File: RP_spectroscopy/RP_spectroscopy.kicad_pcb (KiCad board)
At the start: 2 copper layers, 90.5 x 110 mm, 82 parts, among them J1 Extension connector 1, J2 Extension connector 2, J3 Conn_Coaxial, J4 Conn_Coaxial, J5 Conn_Coaxial, J6 Conn_Coaxial, J7 Conn_01x04_MountingPin, J8 Conn_01x04_MountingPin, U1 AD8603, U2 ADG417BR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

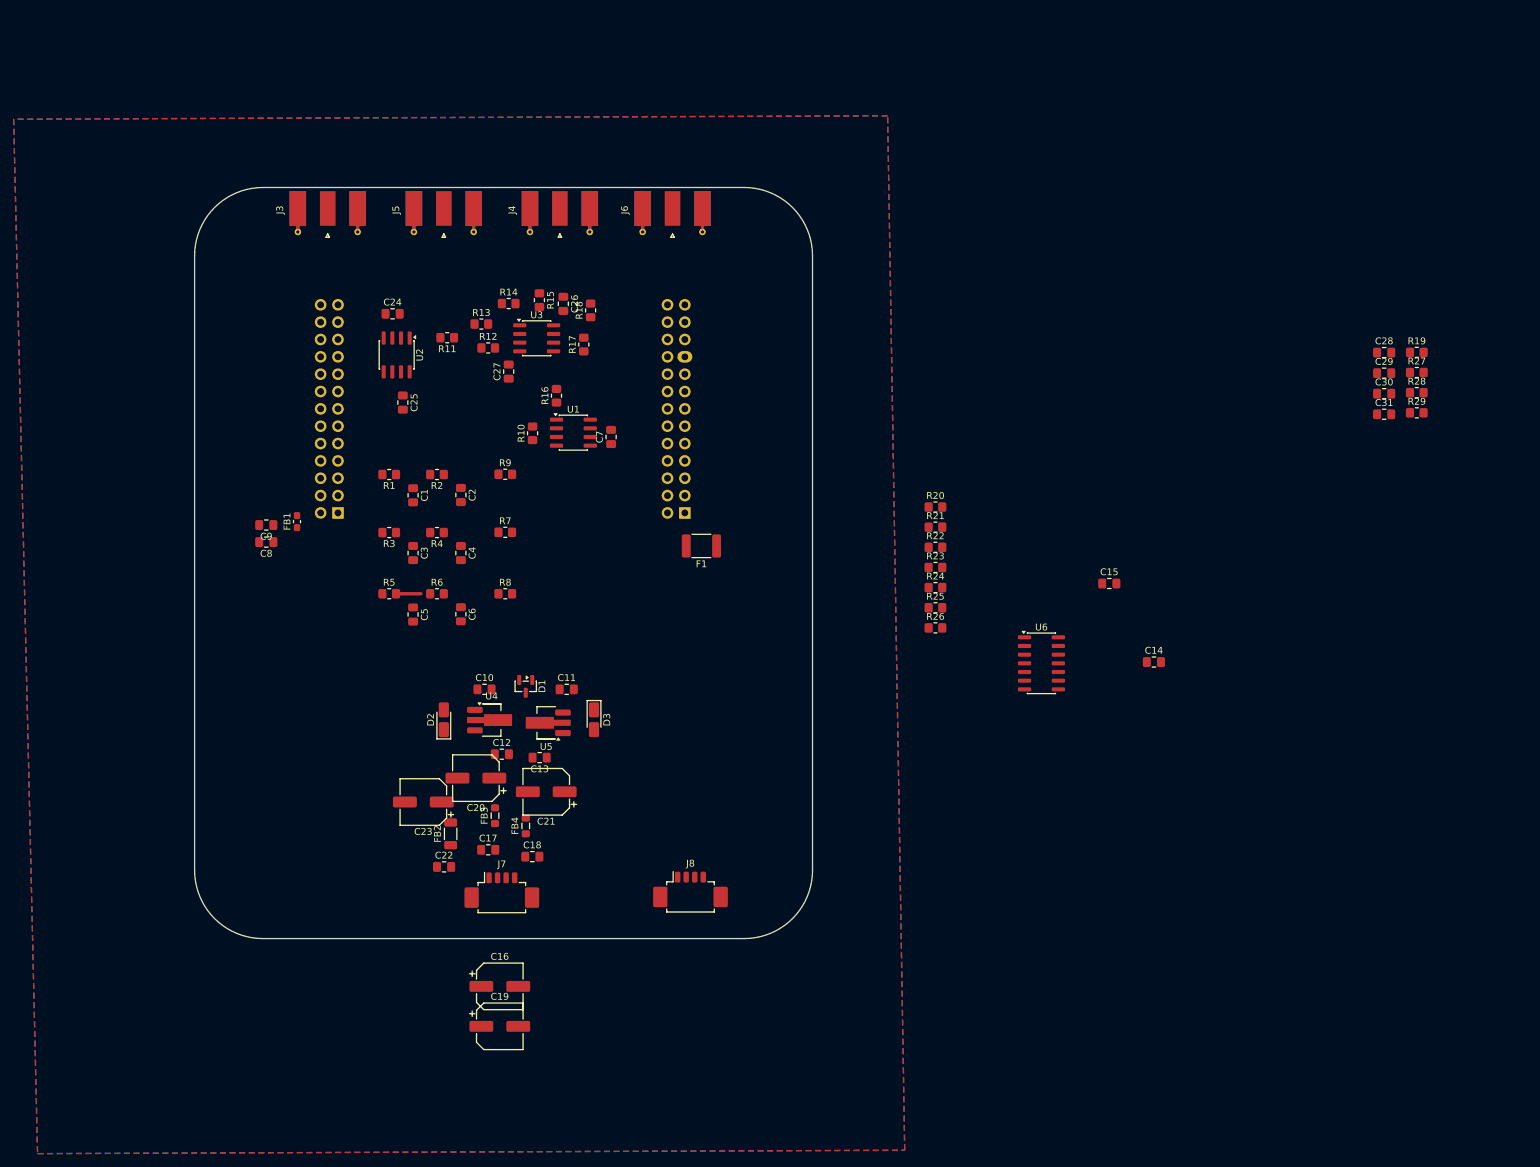
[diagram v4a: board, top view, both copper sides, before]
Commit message: Added the summator parameters. Started to do the wireings
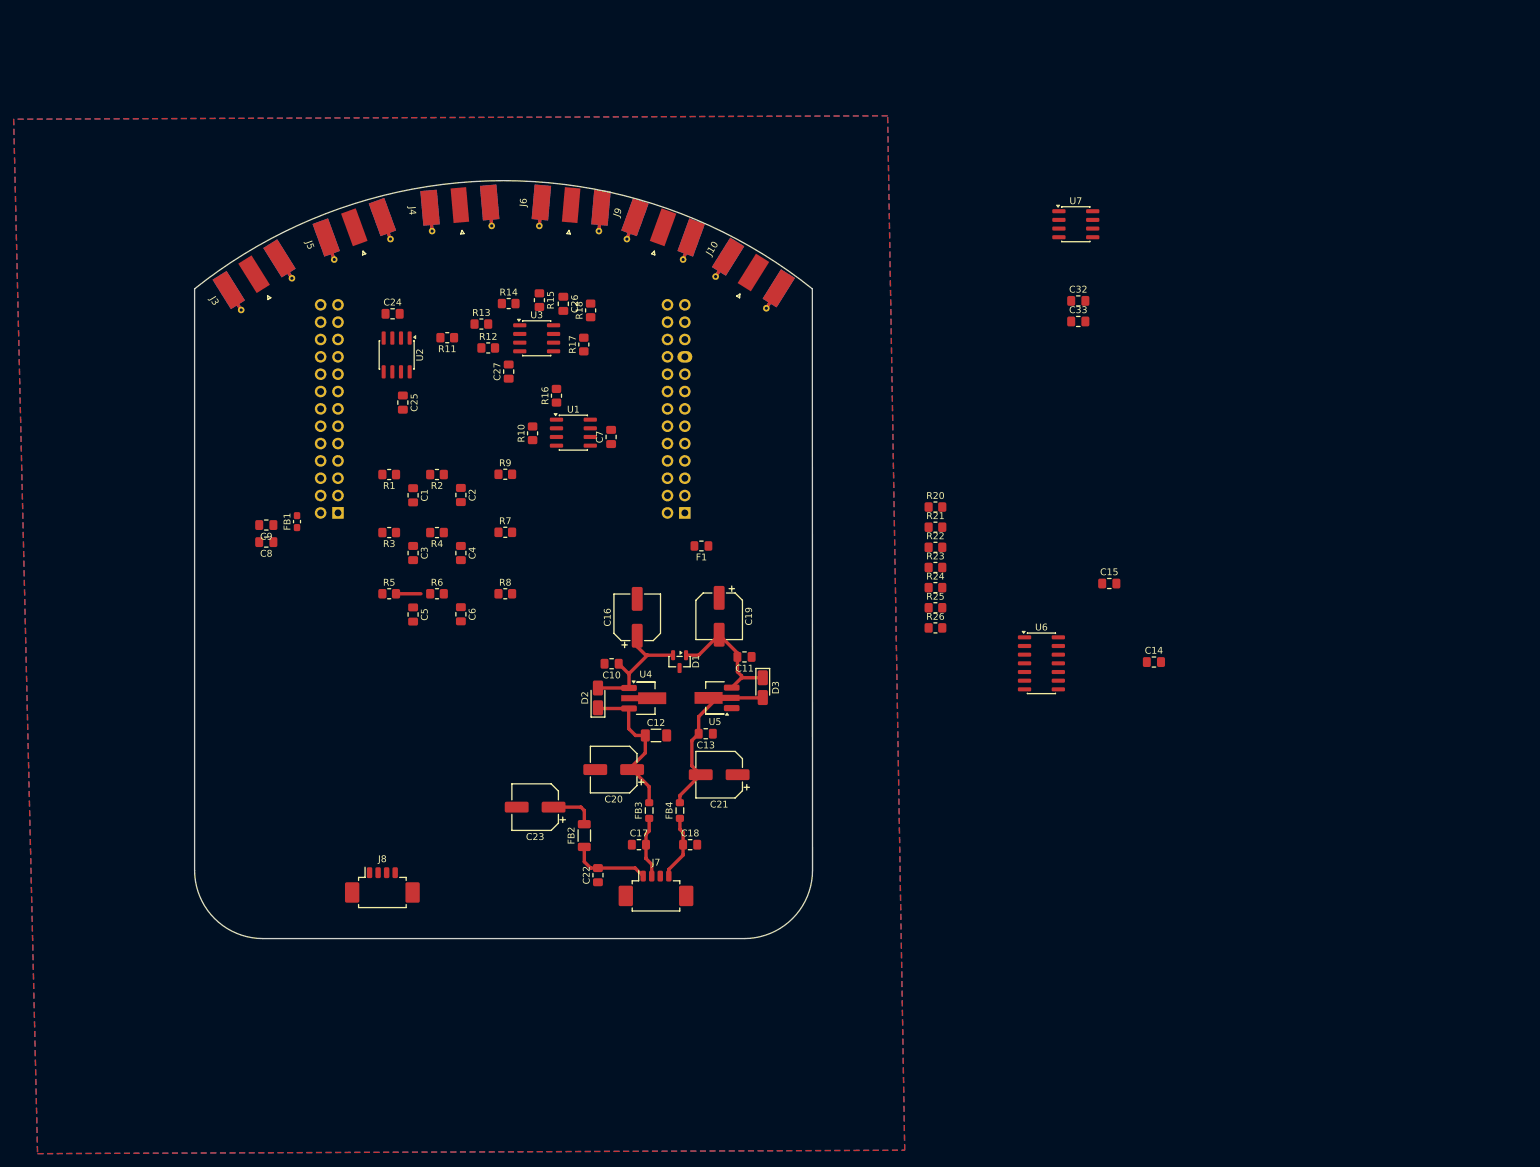
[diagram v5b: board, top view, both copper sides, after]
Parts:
- removed C28, C29, C30, C31: 33n, Capacitor_SMD:C_0805_2012Metric_Pad1.18x1.45mm_HandSolder
- removed R19: 2K55, Resistor_SMD:R_0805_2012Metric_Pad1.20x1.40mm_HandSolder
- removed R27: 365, Resistor_SMD:R_0805_2012Metric_Pad1.20x1.40mm_HandSolder
- removed R28: 1K05, Resistor_SMD:R_0805_2012Metric_Pad1.20x1.40mm_HandSolder
- removed R29: 887, Resistor_SMD:R_0805_2012Metric_Pad1.20x1.40mm_HandSolder
- added C32: 100n, Capacitor_SMD:C_0805_2012Metric_Pad1.18x1.45mm_HandSolder, F.Cu at (219.4, 56.6)
- added C33: 100n, Capacitor_SMD:C_0805_2012Metric_Pad1.18x1.45mm_HandSolder, F.Cu at (219.4, 59.6)
- added J10: Conn_Coaxial, Connector_Coaxial:SMA_Molex_73251-1153_EdgeMount_Horizontal, F.Cu at (170.9, 53.9)
- added J9: Conn_Coaxial, Connector_Coaxial:SMA_Molex_73251-1153_EdgeMount_Horizontal, F.Cu at (158.0, 47.4)
- added U7: DG419DY, Package_SO:SOIC-8_3.9x4.9mm_P1.27mm, F.Cu at (219.1, 45.4)
- C12: footprint Capacitor_SMD:C_0805_2012Metric_Pad1.18x1.45mm_HandSolder -> Capacitor_SMD:C_1206_3216Metric_Pad1.33x1.80mm_HandSolder
- F1: footprint Fuse:Fuse_1812_4532Metric_Pad1.30x3.40mm_HandSolder -> Fuse:Fuse_0805_2012Metric_Pad1.15x1.40mm_HandSolder
- J7, J8: value Conn_01x04_MountingPin -> Molex PicoBlade
- R10: value 20k -> 22k
- R12, R13, R14, R15, R16, R17: value 3k -> 3k3
- R7, R9: value R -> 15k4
- moved C19 68.1 mm to (166.8, 102.8), turned to -90 degrees
- moved C16 57.7 mm to (154.8, 103.0), turned to 90 degrees
- moved J8 45.1 mm to (117.5, 142.8)
- moved C11 26.5 mm to (170.5, 108.8), turned to 180 degrees
- moved C21 25.4 mm to (166.8, 126.0)
- moved D3 25.2 mm to (173.2, 113.2)
- moved U5 25.0 mm to (166.2, 114.8)
- moved C13 24.6 mm to (164.9, 120.0)
- moved C18 23.2 mm to (162.6, 136.2)
- moved D1 22.8 mm to (161.0, 109.4)
- moved D2 22.8 mm to (149.1, 114.8)
- moved U4 22.8 mm to (156.1, 114.8)
- moved C12 22.7 mm to (157.6, 120.2)
- moved FB4 22.7 mm to (161.1, 131.2)
- moved FB3 22.6 mm to (156.6, 131.2)
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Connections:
- J1 pad 3: unconnected-(J1-Pin_3-Pad3) -> Ramp sign
- J1 pad 5: Ramp sign -> Multiplex switch
- J2 pad 20: Not used -> unconnected-(J2-Pin_20-Pad20)
- J4 pad 1: PD -> Differential PD
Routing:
- net Net-(D3-A): track 0.00 -> 25.4 mm
- net Net-(D2-K): track 0.00 -> 22.1 mm
- net +5VA: track 0.00 -> 20.0 mm
- net -5VA: track 0.00 -> 18.9 mm
- net Net-(J7-Pin_1): track 0.00 -> 11.7 mm
- net -15V: track 0.00 -> 9.54 mm
- net +15V: track 0.00 -> 9.02 mm
- net +5V: track 0.00 -> 6.71 mm
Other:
- board size 90.5 x 110 mm -> 90.5 x 111 mm

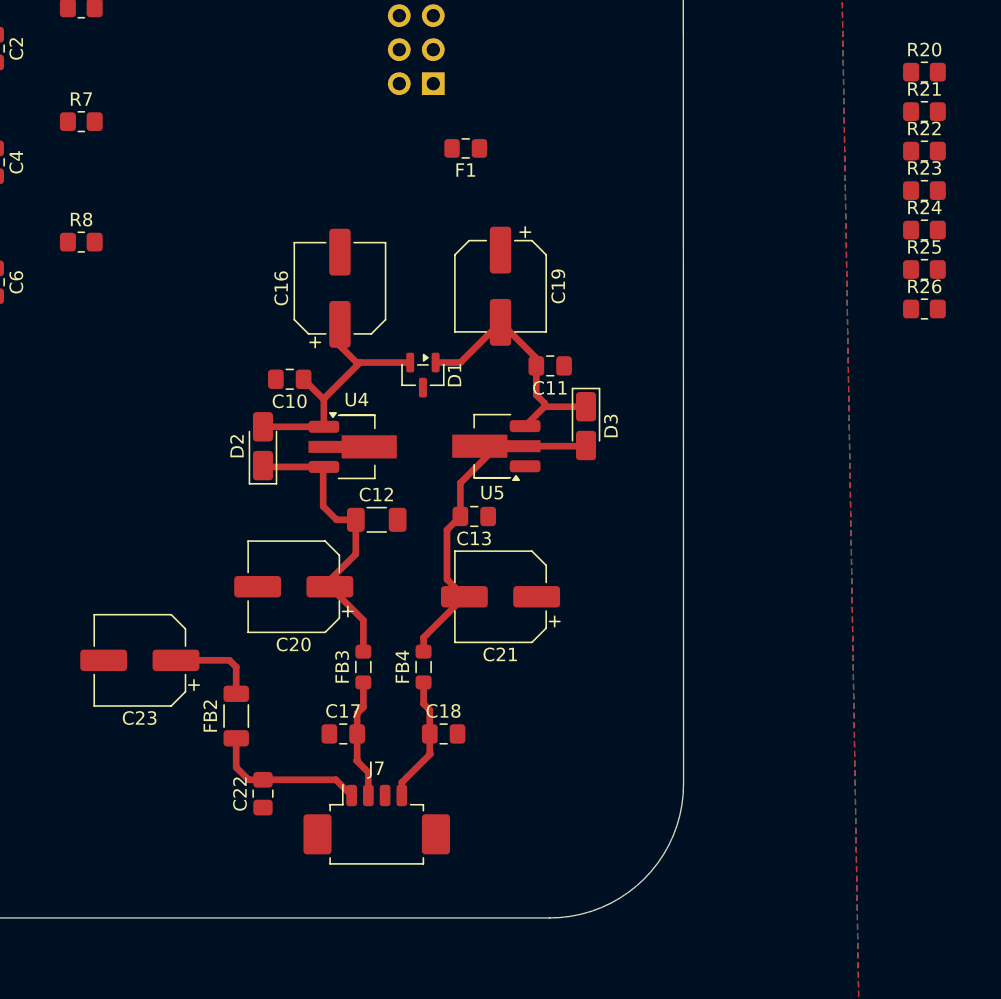
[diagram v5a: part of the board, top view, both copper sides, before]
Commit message: Modified the input power connections in order to have the 5V to power the RP from the correct side
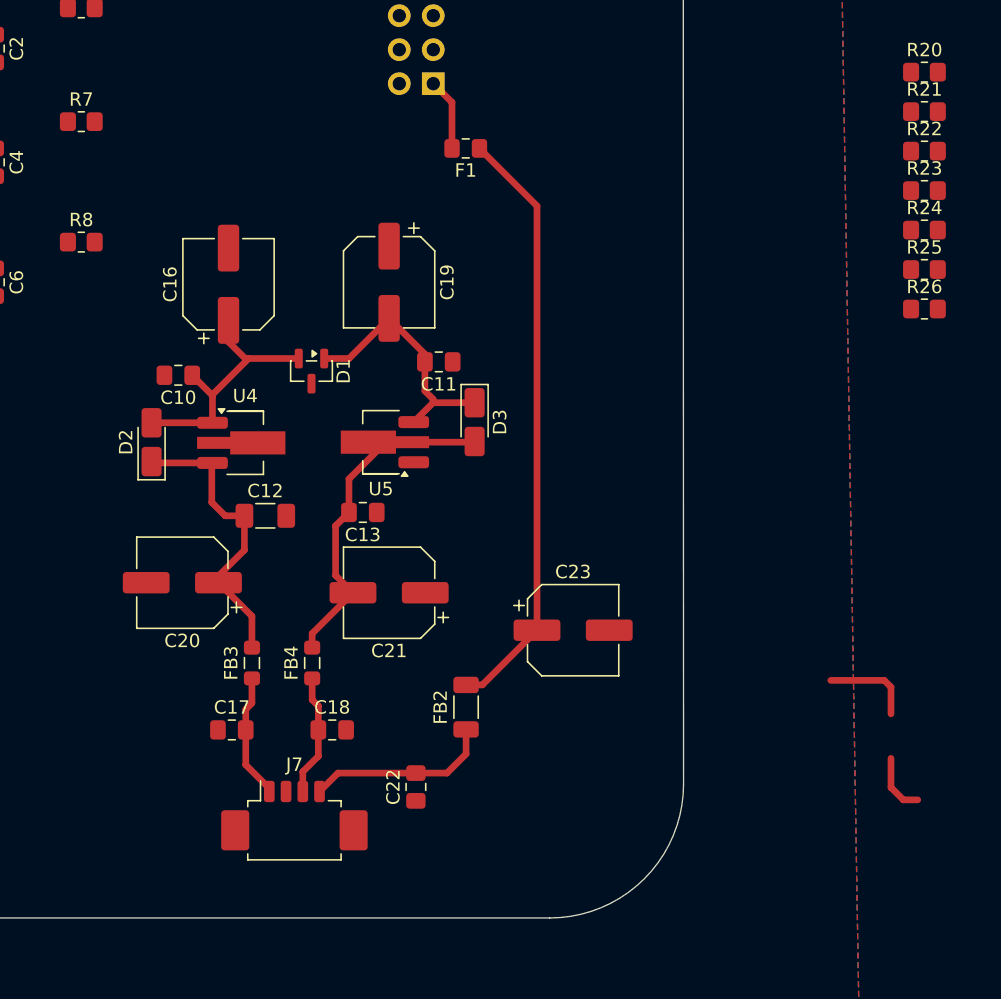
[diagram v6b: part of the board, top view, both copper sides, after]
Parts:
- moved C23 32.5 mm to (172.2, 128.5), turned to 0 degrees
- moved FB2 17.2 mm to (164.2, 134.2)
- moved C22 11.4 mm to (160.5, 140.2)
- moved C13 8.33 mm to (156.5, 119.7)
- moved D1 8.33 mm to (152.7, 109.1)
- moved D3 8.33 mm to (164.9, 113.0)
- moved U5 8.33 mm to (157.9, 114.5)
- moved C17 8.33 mm to (146.8, 135.9)
- moved C18 8.33 mm to (154.2, 135.9)
- moved FB3 8.33 mm to (148.2, 130.9)
- moved FB4 8.33 mm to (152.8, 130.9)
- moved C10 8.33 mm to (142.8, 109.5)
- moved C11 8.33 mm to (162.2, 108.5)
- moved C12 8.33 mm to (149.2, 120.0)
- moved C16 8.33 mm to (146.5, 102.7)
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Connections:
- C22 pad 2: Net-(J7-Pin_1) -> Net-(J7-Pin_4)
- FB2 pad 1: Net-(J7-Pin_1) -> Net-(J7-Pin_4)
- J7 pad 1: Net-(J7-Pin_1) -> +15V
- J7 pad 2: +15V -> GND
- J7 pad 3: GND -> -15V
- J7 pad 4: -15V -> Net-(J7-Pin_4)
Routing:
- net +5V: track 6.71 -> 51.5 mm
- net Net-(J7-Pin_4): track 0.00 -> 18.5 mm
- net Net-(J7-Pin_1): track 11.7 -> 0.00 mm
- net Net-(J2-Pin_1): track 0.00 -> 5.42 mm

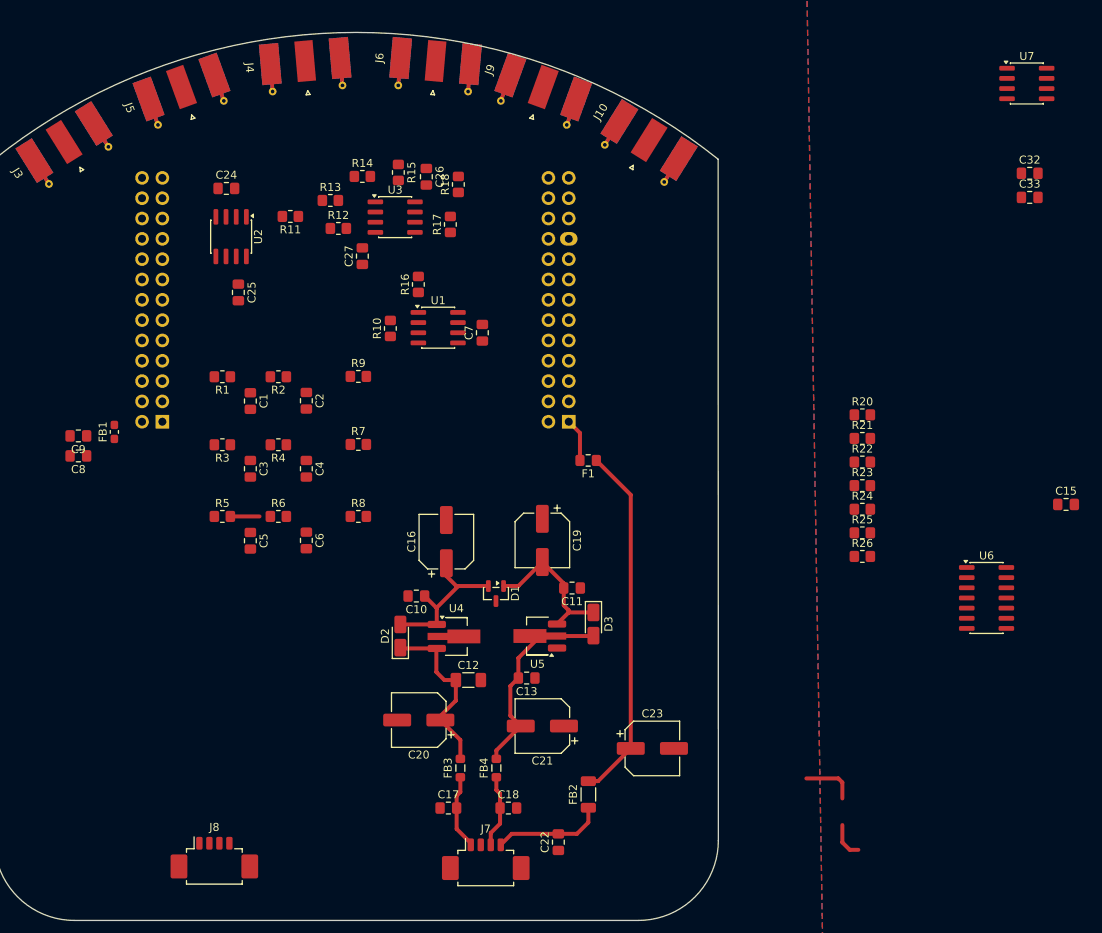
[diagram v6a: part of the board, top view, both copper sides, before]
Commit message: Continued with the wireing of the PCB
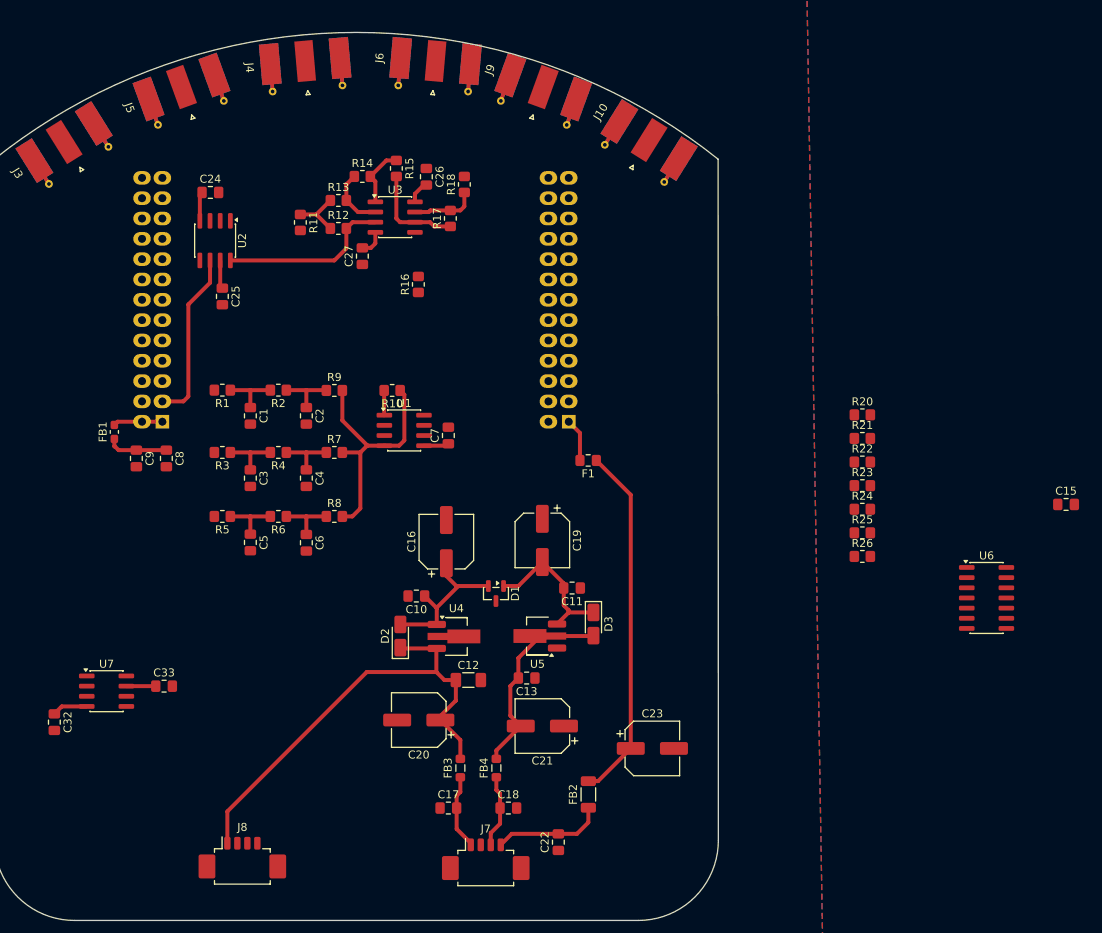
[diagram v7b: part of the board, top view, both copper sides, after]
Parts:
- moved C32 139.9 mm to (97.5, 125.2), turned to -90 degrees
- moved U7 137.9 mm to (104.0, 121.3)
- moved C33 124.3 mm to (111.2, 120.7)
- moved C7 13.5 mm to (146.8, 89.4)
- moved U1 13.5 mm to (141.2, 88.8)
- moved C8 11.0 mm to (111.5, 92.2), turned to -90 degrees
- moved C9 7.78 mm to (107.8, 92.2), turned to -90 degrees
- moved R10 7.75 mm to (139.7, 83.8), turned to 180 degrees
- moved J8 3.50 mm to (121.0, 142.8)
- moved R9 3.47 mm to (132.5, 83.8)
- moved R7 3.16 mm to (132.5, 91.5)
- moved R8 3.00 mm to (132.5, 99.5)
- moved C24 2.06 mm to (117.0, 59.0)
- moved C25 2.06 mm to (118.5, 72.0)
- moved U2 2.06 mm to (117.6, 65.0)
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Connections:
- C12 pad 1: Net-(D2-K) -> +15V
- C13 pad 2: Net-(D3-A) -> -15V
- C17 pad 2: +15V -> Net-(J7-Pin_1)
- C18 pad 1: -15V -> Net-(J7-Pin_3)
- C20 pad 1: Net-(D2-K) -> +15V
- C21 pad 2: Net-(D3-A) -> -15V
- D2 pad 1: Net-(D2-K) -> +15V
- D3 pad 2: Net-(D3-A) -> -15V
- FB3 pad 1: +15V -> Net-(J7-Pin_1)
- FB3 pad 2: Net-(D2-K) -> +15V
- FB4 pad 1: -15V -> Net-(J7-Pin_3)
- FB4 pad 2: Net-(D3-A) -> -15V
- J7 pad 1: +15V -> Net-(J7-Pin_1)
- J7 pad 3: -15V -> Net-(J7-Pin_3)
- U4 pad 3: Net-(D2-K) -> +15V
- U5 pad 2: Net-(D3-A) -> -15V
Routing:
- net +15V: track 9.37 -> 59.4 mm
- net Net-(U1--): track 0.00 -> 32.7 mm
- net Net-(D3-A): track 25.4 -> 0.00 mm
- net Net-(D2-K): track 22.1 -> 0.00 mm
- net Ramp sign: track 0.00 -> 21.6 mm
- net Net-(U3A-+): track 0.00 -> 21.6 mm
- net -15V: track 9.12 -> 25.4 mm
- net Net-(U3B--): track 0.00 -> 12.4 mm
- net +5VA: track 20.0 -> 31.0 mm
- net +3V3: track 0.00 -> 10.8 mm
- net -5VA: track 18.9 -> 29.4 mm
- net Net-(J7-Pin_1): track 0.00 -> 9.37 mm
- net Net-(J7-Pin_3): track 0.00 -> 9.12 mm
- net Net-(R17-Pad2): track 0.00 -> 8.21 mm
- net Net-(U3A--): track 0.00 -> 7.64 mm
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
